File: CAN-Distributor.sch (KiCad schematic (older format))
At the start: 6 parts, among them J1 2p Terminal Block, U1 CL25N8-G

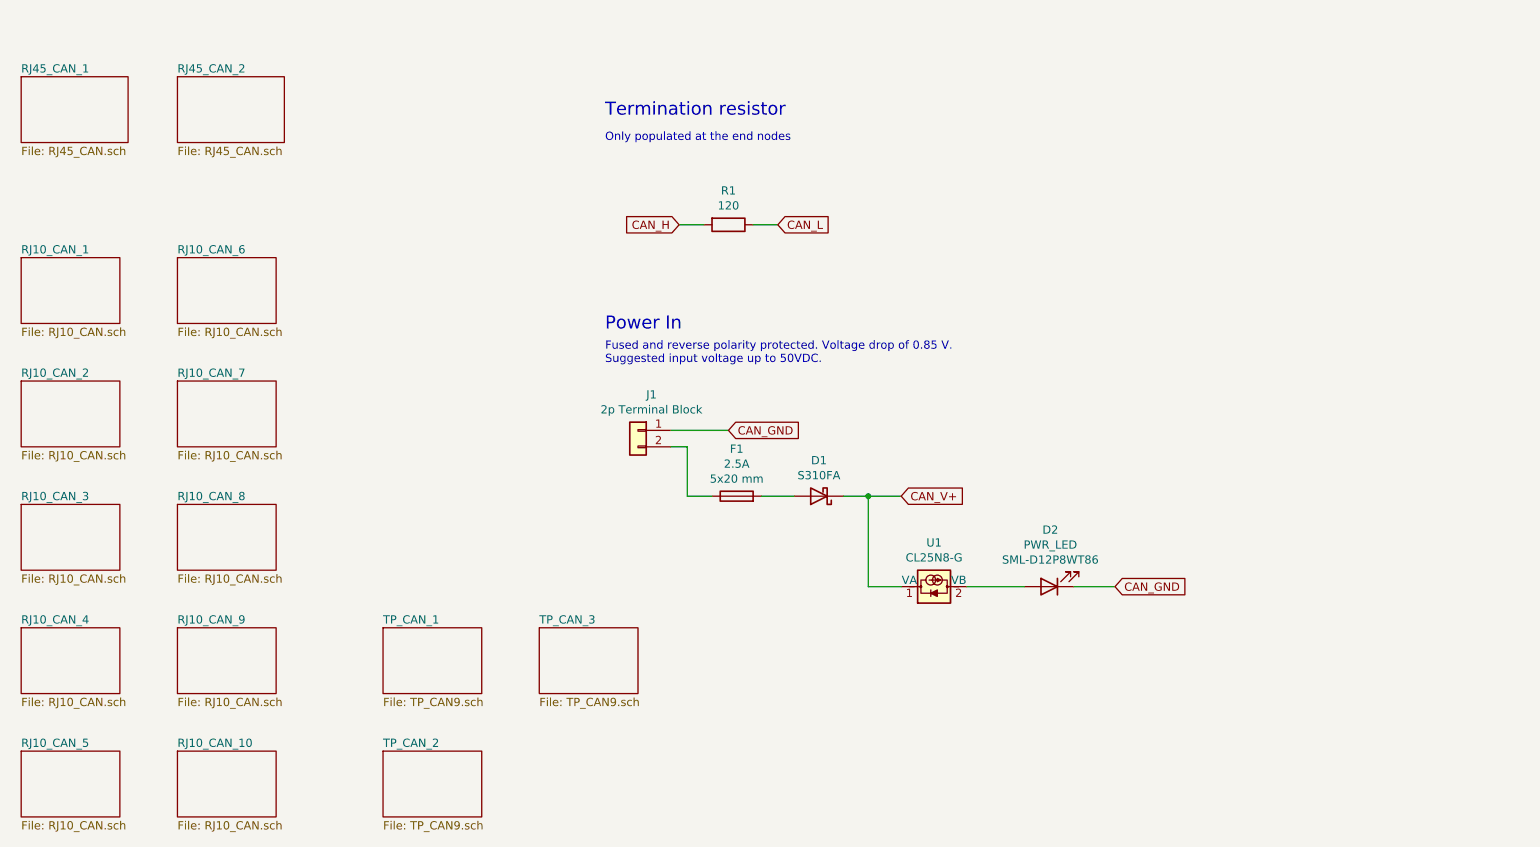
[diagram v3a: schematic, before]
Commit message: Add protection TVS and GDT. Rename TP file.
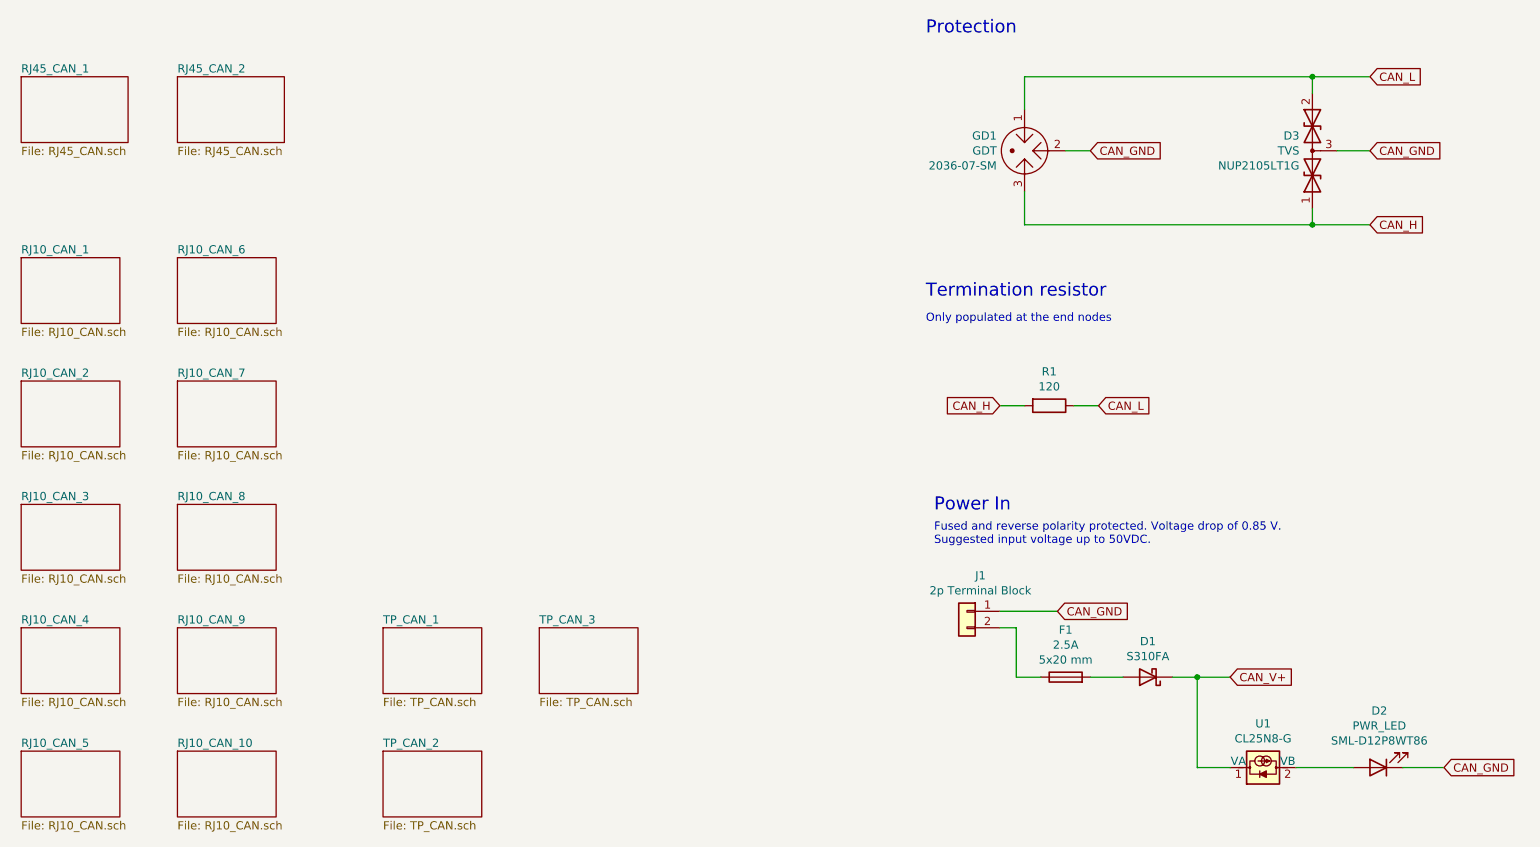
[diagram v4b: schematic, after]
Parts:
- added D3: TVS, Package_TO_SOT_SMD:SOT-23, symbol Device:D_TVS_x2_AAC
- added GD1: GDT, CAN-Distributor:Bourns_Inc.-2036-07-SM-RPLF-MFG, symbol CAN-Distributor:Bourns_2038_GDT
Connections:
- net CAN_GND: now also D3.3 (common), GD1.2
- net CAN_H: now also D3.1 (A1), GD1.3
- net CAN_L: now also D3.2 (A2), GD1.1
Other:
- note added: "Protection"
- moved on the sheet: D1, D2, F1, J1, R1, U1

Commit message: Add additional GND input
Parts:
- J1: value 2p Terminal Block -> 3p Terminal Block; footprint TerminalBlock:TerminalBlock_bornier-2_P5.08mm -> TerminalBlock:TerminalBlock_bornier-3_P5.08mm; symbol Connector_Generic:Conn_01x02 -> Connector_Generic:Conn_01x03
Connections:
- net CAN_GND: now also J1.2 (Pin_2)
- net at F1.1: now also J1.3 (Pin_3); no longer J1.2 (Pin_2)
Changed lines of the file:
@@
 Power In
 $Comp
-L Connector_Generic:Conn_01x02 J1
+L Connector_Generic:Conn_01x03 J1
 U 1 1 60687EFE
 P 7450 5200
-F 0 "J1" H 7368 5417 50  0000 C CNN
-F 1 "2p Terminal Block" H 7368 5326 50  0000 C CNN
-F 2 "TerminalBlock:TerminalBlock_bornier-2_P5.08mm" H 7450 5200 50  0001 C CNN
+F 0 "J1" H 7350 5500 50  0000 C CNN
+F 1 "3p Terminal Block" H 7350 5400 50  0000 C CNN
+F 2 "TerminalBlock:TerminalBlock_bornier-3_P5.08mm" H 7450 5200 50  0001 C CNN
 F 3 "~" H 7450 5200 50  0001 C CNN
 F 4 "~" H 7450 5200 50  0001 C CNN "Farnell"
@@
 $EndComp
 Wire Wire Line
-	7650 5200 8000 5200
+	7650 5200 7900 5200
 $Comp
 L Device:Fuse F1
@@
 Text GLabel 9050 5600 2    50   Input ~ 0
 CAN_V+
-Text GLabel 8000 5200 2    50   Input ~ 0
+Text GLabel 8000 5150 2    50   Input ~ 0
 CAN_GND
 Text Notes 7200 1700 0    79   ~ 0
@@
 F1 "TP_CAN.sch" 50
 $EndSheet
+Wire Wire Line
+	7650 5100 7900 5100
+Wire Wire Line
+	7900 5100 7900 5150
+Wire Wire Line
+	7900 5150 8000 5150
+Connection ~ 7900 5150
+Wire Wire Line
+	7900 5150 7900 5200
 $EndSCHEMATC
